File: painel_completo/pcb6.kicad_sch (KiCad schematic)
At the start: 12 parts, among them J12 Conn_02x05_Odd_Even, J14 Conn_02x02_Odd_Even, SW19 SW_Push_LED, SW20 SW_Push_LED, SW21 SW_Push, SW22 SW_Push_LED

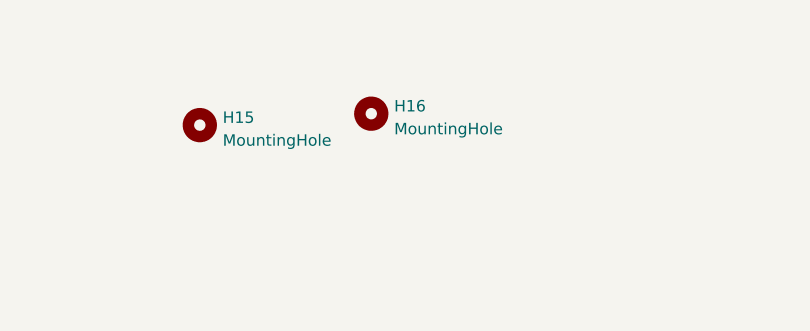
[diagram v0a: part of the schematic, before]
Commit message: adição furos fixação e alteração máscara de componentes
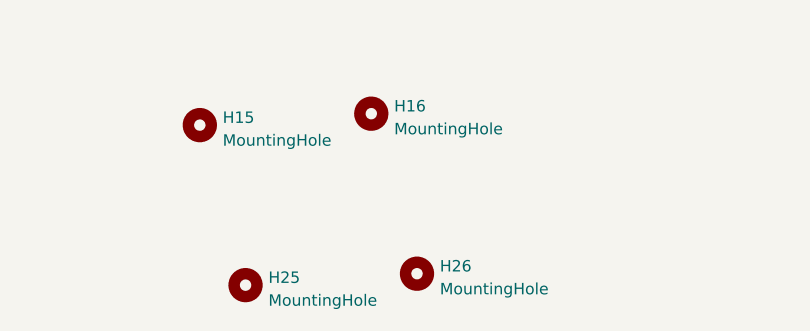
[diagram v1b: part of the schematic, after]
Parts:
- added H25, H26: MountingHole, MountingHole:MountingHole_3.2mm_M3, symbol Mechanical:MountingHole
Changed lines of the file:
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@@
     (pin "2")
+  )
+  (symbol (lib_id "Mechanical:MountingHole") (at 119.38 158.75 0) (unit 1)
+    (in_bom yes) (on_board yes) (fields_autoplaced)
+    (property "Reference" "H25" (id 0) (at 121.92 157.9153 0)
+      (effects (font (size 1.27 1.27)) (justify left))
+    )
+    (property "Value" "MountingHole" (id 1) (at 121.92 160.4522 0)
+      (effects (font (size 1.27 1.27)) (justify left))
+    )
+    (property "Footprint" "MountingHole:MountingHole_3.2mm_M3" (id 2) (at 119.38 158.75 0)
+      (effects (font (size 1.27 1.27)) hide)
+    )
+    (property "Datasheet" "~" (id 3) (at 119.38 158.75 0)
+      (effects (font (size 1.27 1.27)) hide)
+    )
   )
   (symbol (lib_id "Connector_Generic:Conn_02x02_Odd_Even") (at 218.44 124.46 0) (unit 1)
@@
     (pin "4")
   )
+  (symbol (lib_id "Mechanical:MountingHole") (at 138.43 157.48 0) (unit 1)
+    (in_bom yes) (on_board yes) (fields_autoplaced)
+    (property "Reference" "H26" (id 0) (at 140.97 156.6453 0)
+      (effects (font (size 1.27 1.27)) (justify left))
+    )
+    (property "Value" "MountingHole" (id 1) (at 140.97 159.1822 0)
+      (effects (font (size 1.27 1.27)) (justify left))
+    )
+    (property "Footprint" "MountingHole:MountingHole_3.2mm_M3" (id 2) (at 138.43 157.48 0)
+      (effects (font (size 1.27 1.27)) hide)
+    )
+    (property "Datasheet" "~" (id 3) (at 138.43 157.48 0)
+      (effects (font (size 1.27 1.27)) hide)
+    )
+  )
   (symbol (lib_id "Switch:SW_Push_LED") (at 187.96 97.79 0) (unit 1)
